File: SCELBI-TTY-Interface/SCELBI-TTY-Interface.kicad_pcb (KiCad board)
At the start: 2 copper layers, 114.3 x 85.1 mm, 12 parts, among them J1 Edge44

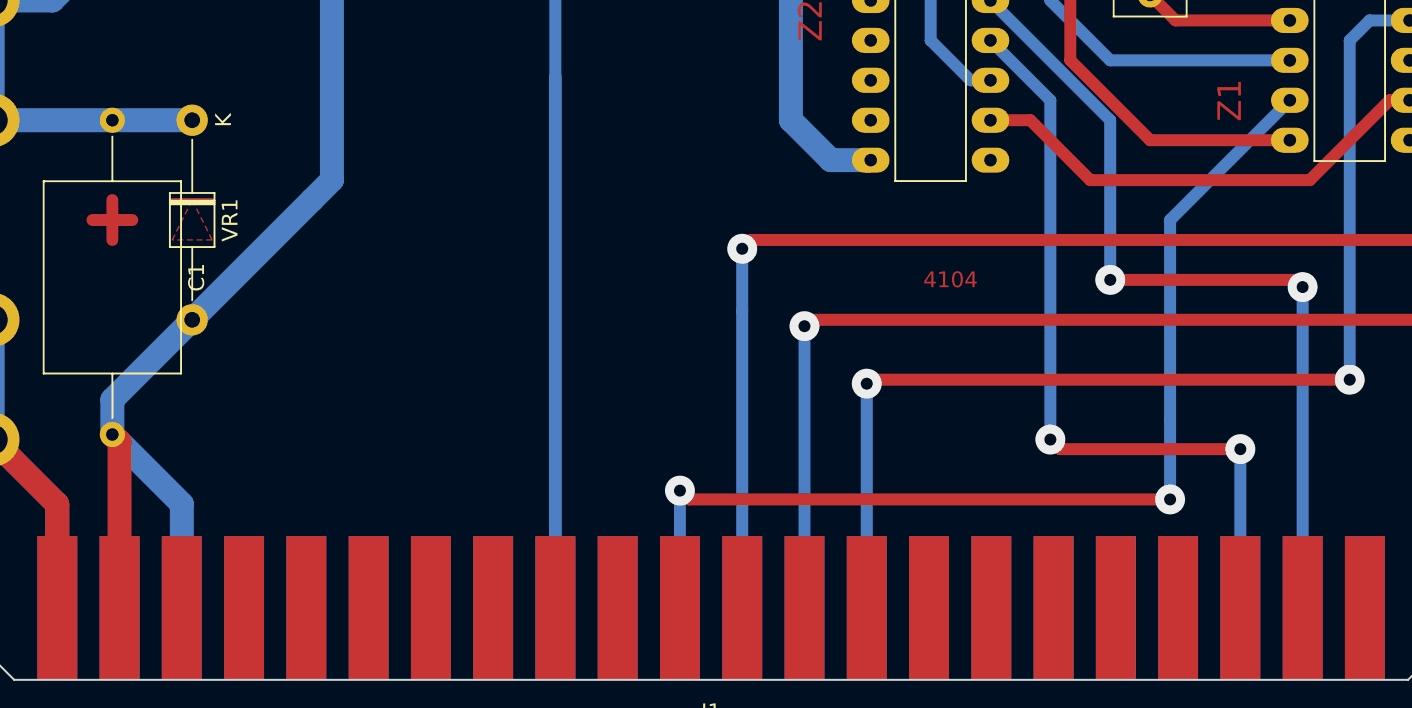
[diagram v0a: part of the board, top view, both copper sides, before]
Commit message: Swap strobe/tx, widen drill for supply components, relabel control signals
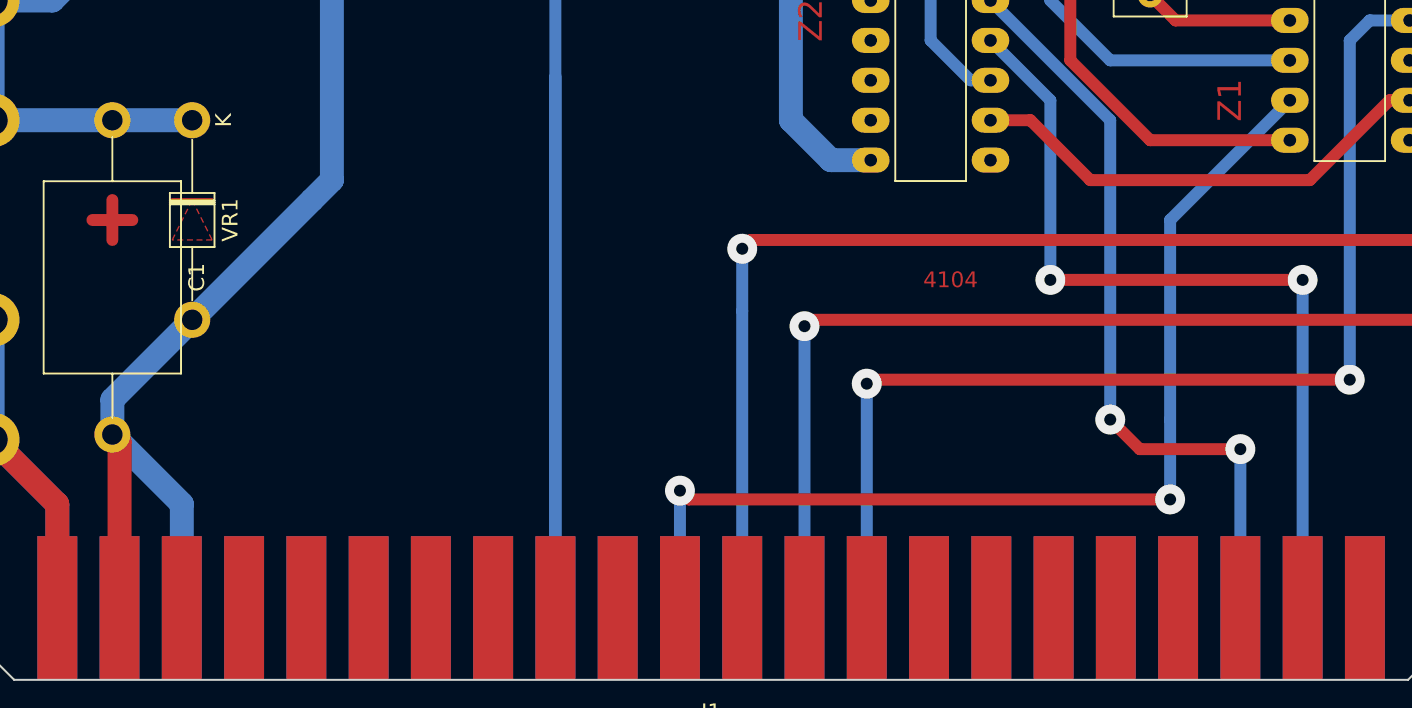
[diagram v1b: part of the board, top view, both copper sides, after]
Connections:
- Z2 pad 11: /Tx -> /STRB
- Z2 pad 12: /STRB -> /Tx
